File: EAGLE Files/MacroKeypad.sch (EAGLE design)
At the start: 13 parts, among them IC2 ATMEGA32U4-MU, SW1 CHERRY-MX, SW2 CHERRY-MX, SW3 CHERRY-MX, SW4 CHERRY-MX, SW5 CHERRY-MX, SW6 CHERRY-MX

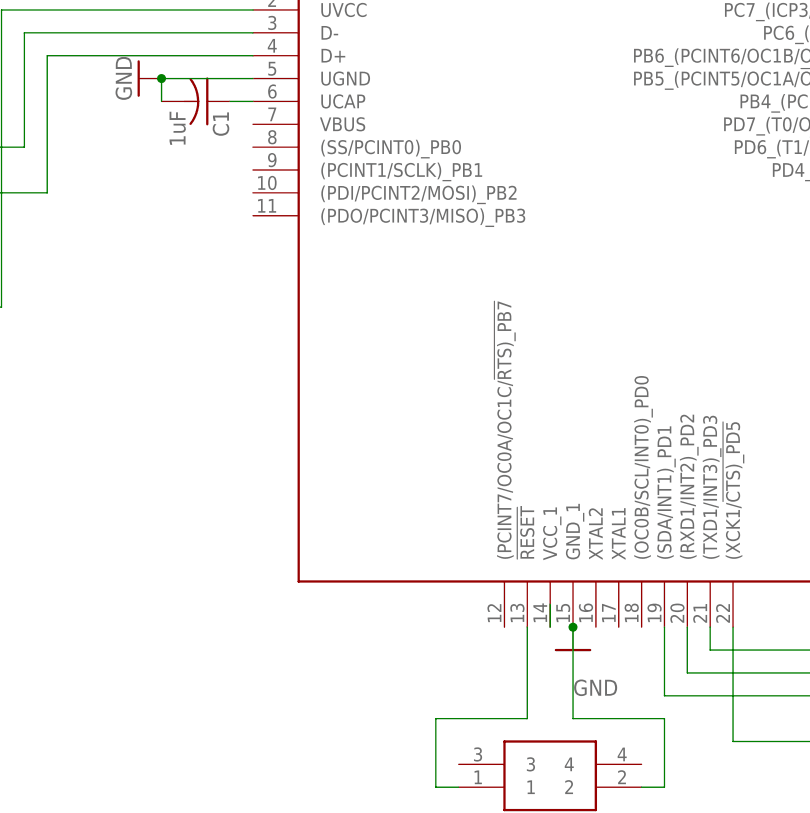
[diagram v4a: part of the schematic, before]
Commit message: Add programming pads
Also added the BOM as it was missing
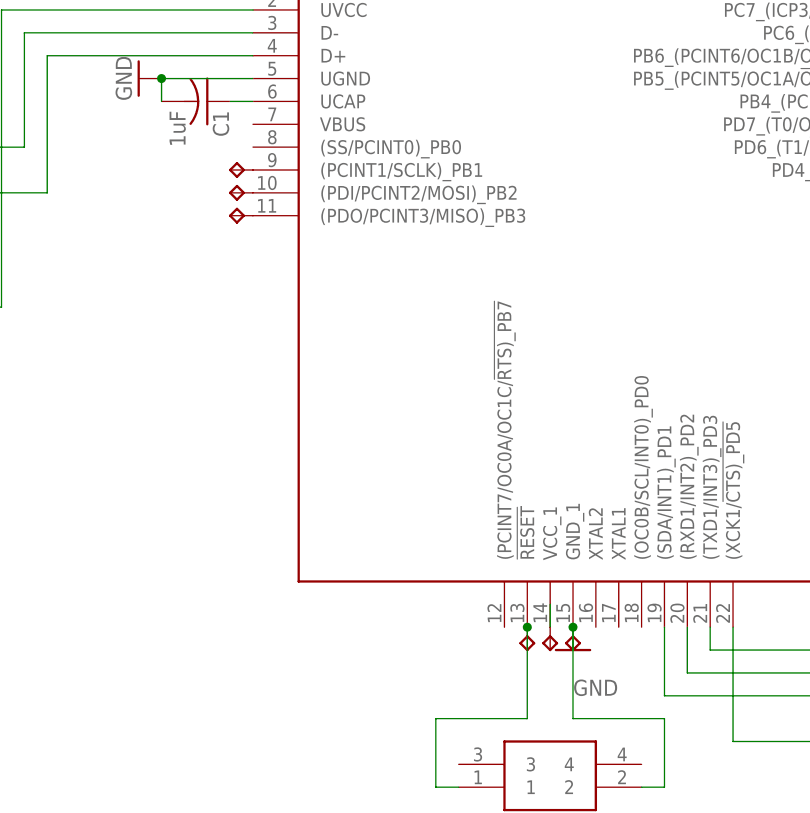
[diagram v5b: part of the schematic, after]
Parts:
- added 5V, GND, MISO, MOSI, RST, SCLK: TPTP17R, testpad:TPTP17R
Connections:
- new net MISO: IC2.(PDO/PCINT3/MISO)_PB3, MISO.TP
- new net MOSI: IC2.(PDI/PCINT2/MOSI)_PB2, MOSI.TP
- new net SCLK: IC2.(PCINT1/SCLK)_PB1, SCLK.TP
- net GND: now also GND.TP
- net RESET: now also RST.TP
- net VCC: now also 5V.TP
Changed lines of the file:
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@@
 <part name="GND7" library="supply1" library_urn="urn:adsk.eagle:library:371" deviceset="GND" device=""/>
 <part name="RESET" library="SamacSys_Parts" deviceset="LL3303F065QG" device=""/>
+<part name="RST" library="testpad" library_urn="urn:adsk.eagle:library:385" deviceset="TP" device="TP17R" package3d_urn="urn:adsk.eagle:package:27971/1"/>
+<part name="5V" library="testpad" library_urn="urn:adsk.eagle:library:385" deviceset="TP" device="TP17R" package3d_urn="urn:adsk.eagle:package:27971/1"/>
+<part name="GND" library="testpad" library_urn="urn:adsk.eagle:library:385" deviceset="TP" device="TP17R" package3d_urn="urn:adsk.eagle:package:27971/1"/>
+<part name="MISO" library="testpad" library_urn="urn:adsk.eagle:library:385" deviceset="TP" device="TP17R" package3d_urn="urn:adsk.eagle:package:27971/1"/>
+<part name="MOSI" library="testpad" library_urn="urn:adsk.eagle:library:385" deviceset="TP" device="TP17R" package3d_urn="urn:adsk.eagle:package:27971/1"/>
+<part name="SCLK" library="testpad" library_urn="urn:adsk.eagle:library:385" deviceset="TP" device="TP17R" package3d_urn="urn:adsk.eagle:package:27971/1"/>
 </parts>
 <sheets>
@@
 <attribute name="NAME" x="-100.33" y="25.4" size="1.778" layer="95" align="center-left"/>
 </instance>
+<instance part="RST" gate="G$1" x="-99.06" y="45.72" smashed="yes" rot="R180">
+<attribute name="TP_SIGNAL_NAME" x="-100.33" y="46.99" size="1.778" layer="97" rot="R180"/>
+</instance>
+<instance part="5V" gate="G$1" x="-96.52" y="45.72" smashed="yes" rot="R180">
+<attribute name="TP_SIGNAL_NAME" x="-97.79" y="46.99" size="1.778" layer="97" rot="R180"/>
+</instance>
+<instance part="GND" gate="G$1" x="-93.98" y="45.72" smashed="yes" rot="R180">
+<attribute name="TP_SIGNAL_NAME" x="-95.25" y="46.99" size="1.778" layer="97" rot="R180"/>
+</instance>
+<instance part="MISO" gate="G$1" x="-132.08" y="93.98" smashed="yes" rot="R90">
+<attribute name="TP_SIGNAL_NAME" x="-130.81" y="95.25" size="1.778" layer="97" rot="R90"/>
+</instance>
+<instance part="MOSI" gate="G$1" x="-132.08" y="96.52" smashed="yes" rot="R90">
+<attribute name="TP_SIGNAL_NAME" x="-130.81" y="97.79" size="1.778" layer="97" rot="R90"/>
+</instance>
+<instance part="SCLK" gate="G$1" x="-132.08" y="99.06" smashed="yes" rot="R90">
+<attribute name="TP_SIGNAL_NAME" x="-130.81" y="100.33" size="1.778" layer="97" rot="R90"/>
+</instance>
 </instances>
 <busses>
@@
 <wire x1="-93.98" y1="38.1" x2="-93.98" y2="48.26" width="0.1524" layer="91"/>
 <junction x="-93.98" y="48.26"/>
+<pinref part="GND" gate="G$1" pin="TP"/>
 </segment>
 <segment>
@@
 <pinref part="IC2" gate="G$1" pin="VCC_1"/>
 <wire x1="-96.52" y1="48.26" x2="-96.52" y2="50.8" width="0.1524" layer="91"/>
+<pinref part="5V" gate="G$1" pin="TP"/>
 </segment>
 </net>
@@
 <wire x1="-109.22" y1="38.1" x2="-109.22" y2="30.48" width="0.1524" layer="91"/>
 <wire x1="-109.22" y1="30.48" x2="-106.68" y2="30.48" width="0.1524" layer="91"/>
+<pinref part="RST" gate="G$1" pin="TP"/>
+<junction x="-99.06" y="48.26"/>
+</segment>
+</net>
+<net name="MISO" class="0">
+<segment>
+<pinref part="IC2" gate="G$1" pin="(PDO/PCINT3/MISO)_PB3"/>
+<pinref part="MISO" gate="G$1" pin="TP"/>
+</segment>
+</net>
+<net name="MOSI" class="0">
+<segment>
+<pinref part="IC2" gate="G$1" pin="(PDI/PCINT2/MOSI)_PB2"/>
+<pinref part="MOSI" gate="G$1" pin="TP"/>
+</segment>
+</net>
+<net name="SCLK" class="0">
+<segment>
+<pinref part="IC2" gate="G$1" pin="(PCINT1/SCLK)_PB1"/>
+<pinref part="SCLK" gate="G$1" pin="TP"/>
 </segment>
 </net>
@@
 will not be understood (or retained) with this version.
 </note>
+<note version="8.3" severity="warning">
+Since Version 8.3, EAGLE supports the association of 3D packages
+with devices in libraries, schematics, and board files. Those 3D
+packages will not be understood (or retained) with this version.
+</note>
 </compatibility>

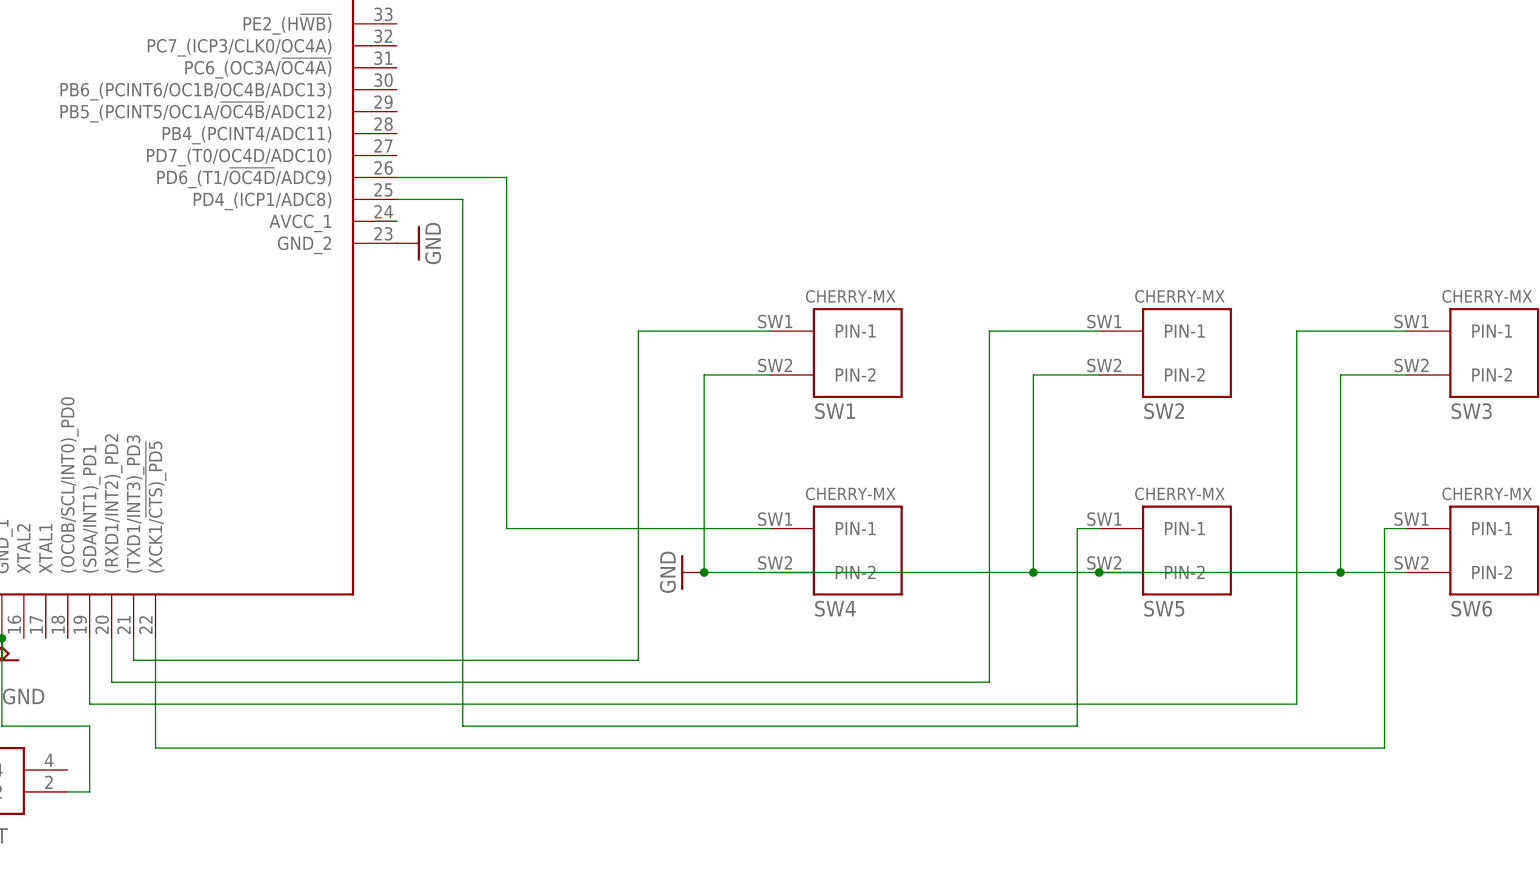
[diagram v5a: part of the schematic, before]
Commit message: Fix switch 6 and add switch pinout
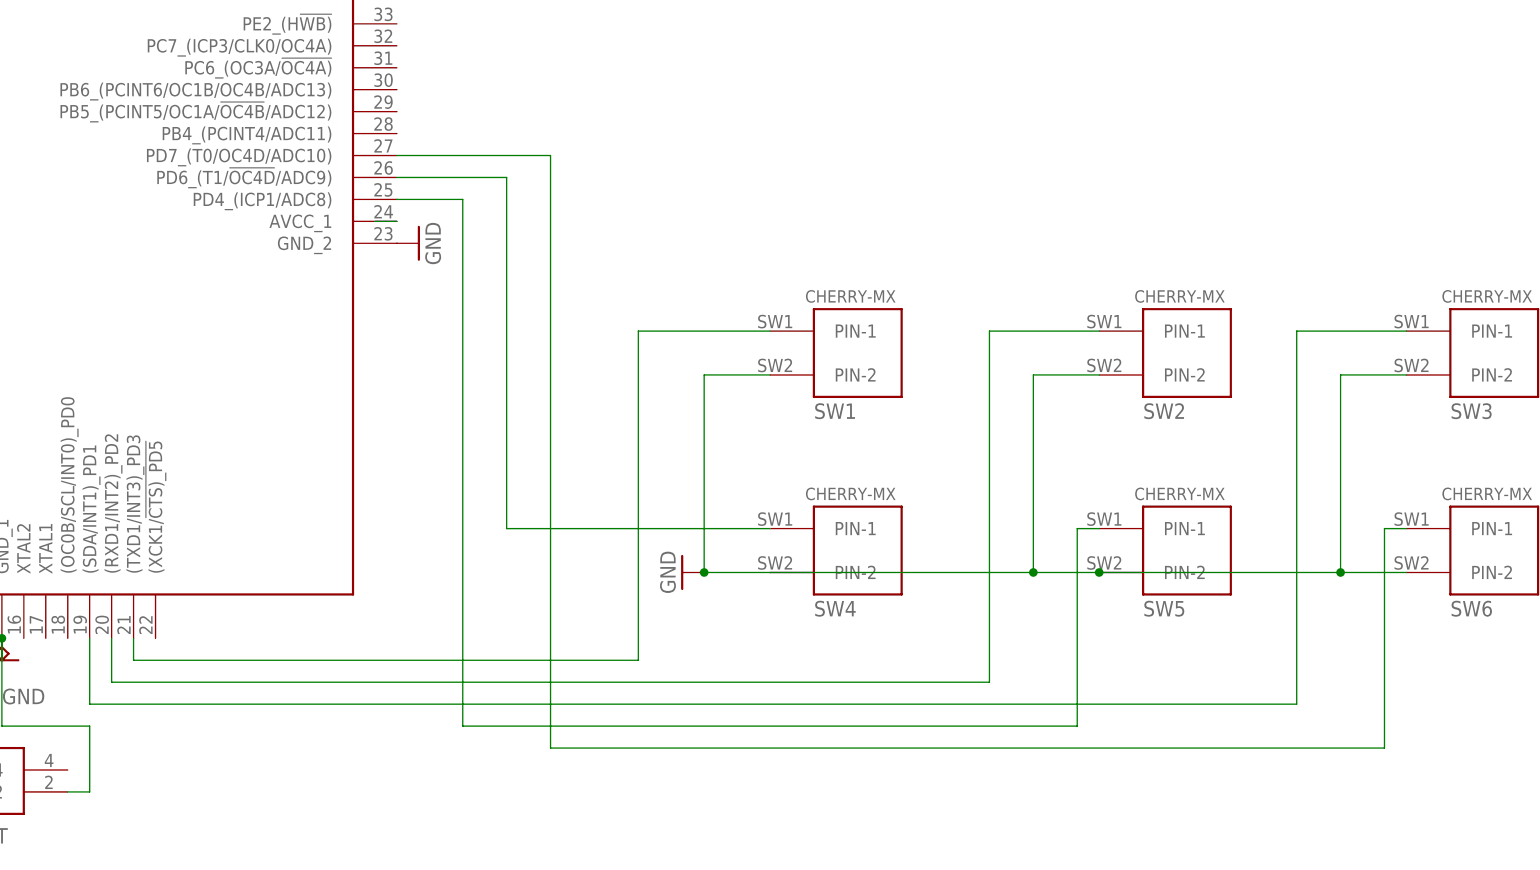
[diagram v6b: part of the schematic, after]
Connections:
- net SW6: now also IC2.PD7_(T0/OC4D/ADC10); no longer IC2.(XCK1/!CTS)_PD5
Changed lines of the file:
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@@
 <wire x1="68.58" y1="60.96" x2="66.04" y2="60.96" width="0.1524" layer="91"/>
 <wire x1="66.04" y1="60.96" x2="66.04" y2="35.56" width="0.1524" layer="91"/>
-<wire x1="66.04" y1="35.56" x2="-76.2" y2="35.56" width="0.1524" layer="91"/>
-<pinref part="IC2" gate="G$1" pin="(XCK1/!CTS)_PD5"/>
-<wire x1="-76.2" y1="35.56" x2="-76.2" y2="48.26" width="0.1524" layer="91"/>
+<wire x1="66.04" y1="35.56" x2="-30.48" y2="35.56" width="0.1524" layer="91"/>
+<pinref part="IC2" gate="G$1" pin="PD7_(T0/OC4D/ADC10)"/>
+<wire x1="-48.26" y1="104.14" x2="-30.48" y2="104.14" width="0.1524" layer="91"/>
+<wire x1="-30.48" y1="104.14" x2="-30.48" y2="35.56" width="0.1524" layer="91"/>
 </segment>
 </net>
